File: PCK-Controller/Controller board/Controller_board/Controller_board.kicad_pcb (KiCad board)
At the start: 2 copper layers, 2 parts, among them SW1 SW_Push, U1 EC10E1260507

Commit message: Dimensions draft
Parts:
- added BT1: Battery_Cell, Battery:BatteryHolder_Keystone_1042_1x18650, F.Cu at (220.5, 100.0)
- added D1: LED, LED_SMD:LED_0603_1608Metric, B.Cu at (152.9, 124.6)
- added D10: LED, LED_SMD:LED_0603_1608Metric, B.Cu at (172.2, 135.6)
- added D11: LED, LED_SMD:LED_0603_1608Metric, B.Cu at (146.1, 137.5)
- added D12: LED, LED_SMD:LED_0603_1608Metric, B.Cu at (120.0, 135.6)
- added D13: LED, LED_SMD:LED_0603_1608Metric, B.Cu at (93.5, 135.6)
- added D14: LED, LED_SMD:LED_0603_1608Metric, B.Cu at (83.5, 114.8)
- added D15: LED, LED_SMD:LED_0603_1608Metric, B.Cu at (83.5, 66.2)
- added D2: LED, LED_SMD:LED_0603_1608Metric, B.Cu at (148.4, 124.6)
- added D3: LED, LED_SMD:LED_0603_1608Metric, B.Cu at (143.9, 124.6)
- added D4: LED, LED_SMD:LED_0603_1608Metric, B.Cu at (139.4, 124.6)
- added D5: LED, LED_SMD:LED_0603_1608Metric, B.Cu at (208.8, 66.2)
- added D6: LED, LED_SMD:LED_0603_1608Metric, B.Cu at (208.8, 82.8)
- added D7: LED, LED_SMD:LED_0603_1608Metric, B.Cu at (208.8, 98.2)
- added D8: LED, LED_SMD:LED_0603_1608Metric, B.Cu at (208.8, 114.8)
- added D9: LED, LED_SMD:LED_0603_1608Metric, B.Cu at (198.8, 135.6)
- added H1: MountingHole_Pad, MountingHole:MountingHole_3.2mm_M3_DIN965_Pad, F.Cu at (71.8, 55.6)
- added H10: MountingHole_Pad, MountingHole:MountingHole_3.2mm_M3_DIN965_Pad, F.Cu at (185.5, 124.5)
- added H11: MountingHole_Pad, MountingHole:MountingHole_3.2mm_M3_DIN965_Pad, F.Cu at (228.2, 144.4)
- added H2: MountingHole_Pad, MountingHole:MountingHole_3.2mm_M3_DIN965_Pad, F.Cu at (110.1, 56.5)
- added H3: MountingHole_Pad, MountingHole:MountingHole_3.2mm_M3_DIN965_Pad, F.Cu at (147.6, 56.5)
- added H4: MountingHole_Pad, MountingHole:MountingHole_3.2mm_M3_DIN965_Pad, F.Cu at (185.1, 56.5)
- added H5: MountingHole_Pad, MountingHole:MountingHole_3.2mm_M3_DIN965_Pad, F.Cu at (228.2, 55.6)
- added H6: MountingHole_Pad, MountingHole:MountingHole_3.2mm_M3_DIN965_Pad, F.Cu at (71.8, 144.4)
- added H7: MountingHole_Pad, MountingHole:MountingHole_3.2mm_M3_DIN965_Pad, F.Cu at (106.8, 124.5)
- added H8: MountingHole_Pad, MountingHole:MountingHole_3.2mm_M3_DIN965_Pad, F.Cu at (132.8, 145.4)
- added H9: MountingHole_Pad, MountingHole:MountingHole_3.2mm_M3_DIN965_Pad, F.Cu at (159.5, 145.4)
- added J1: Conn_01x40, FPC_P0.50mm_Horizontal_40P:FPC_P0.50mm_Horizontal_40P, F.Cu at (178.0, 90.5)
- added J2: Conn_01x06, FPC_P0.50mm_Horizontal_40P:Hirose_FH12-6S-0.5SH_1x06-1MP_P0.50mm_Horizontal, F.Cu at (184.5, 81.0)
- added J3: RJE05-166-1310, SamacSys_Parts.pretty:RJE051661310, F.Cu at (78.9, 135.3)
- added J4: USB_C_Receptacle_USB2.0_14P, Connector_USB:USB_C_Receptacle_HCTL_HC-TYPE-C-16P-01A, F.Cu at (82.1, 52.8)
- added SW10: SW_Push, Button_Switch_SMD:SW_SPST_PTS645Sx43SMTR92, B.Cu at (91.2, 114.8)
- added SW11: SW_Push, Button_Switch_SMD:SW_SPST_PTS645Sx43SMTR92, B.Cu at (91.2, 66.2)
- added SW2: SW_Push, Button_Switch_SMD:SW_SPST_PTS645Sx43SMTR92, B.Cu at (201.1, 66.2)
- added SW3: SW_Push, Button_Switch_SMD:SW_SPST_PTS645Sx43SMTR92, B.Cu at (201.1, 82.8)
- added SW4: SW_Push, Button_Switch_SMD:SW_SPST_PTS645Sx43SMTR92, B.Cu at (201.1, 98.2)
- added SW5: SW_Push, Button_Switch_SMD:SW_SPST_PTS645Sx43SMTR92, B.Cu at (201.1, 114.8)
- added SW6: SW_Push, Button_Switch_SMD:SW_SPST_PTS645Sx43SMTR92, B.Cu at (198.8, 127.1)
- added SW7: SW_Push, Button_Switch_SMD:SW_SPST_PTS645Sx43SMTR92, B.Cu at (172.2, 127.1)
- added SW8: SW_Push, Button_Switch_SMD:SW_SPST_PTS645Sx43SMTR92, B.Cu at (120.0, 127.1)
- added SW9: SW_Push, Button_Switch_SMD:SW_SPST_PTS645Sx43SMTR92, B.Cu at (93.5, 127.1)
- SW1: footprint SamacSys_Parts.pretty:EVQP0E07K -> Button_Switch_SMD:SW_SPST_PTS645Sx43SMTR92; moved to B.Cu
- U1: value EC10E1260507 -> STM32U575VITx; footprint SamacSys_Parts.pretty:EC10E1260507 -> Package_QFP:LQFP-100_14x14mm_P0.5mm
- moved SW1 60.8 mm to (146.1, 129.5), turned to 0 degrees
- moved U1 31.8 mm to (125.3, 91.1)
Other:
- board outline added: 162.5 x 99.8 mm

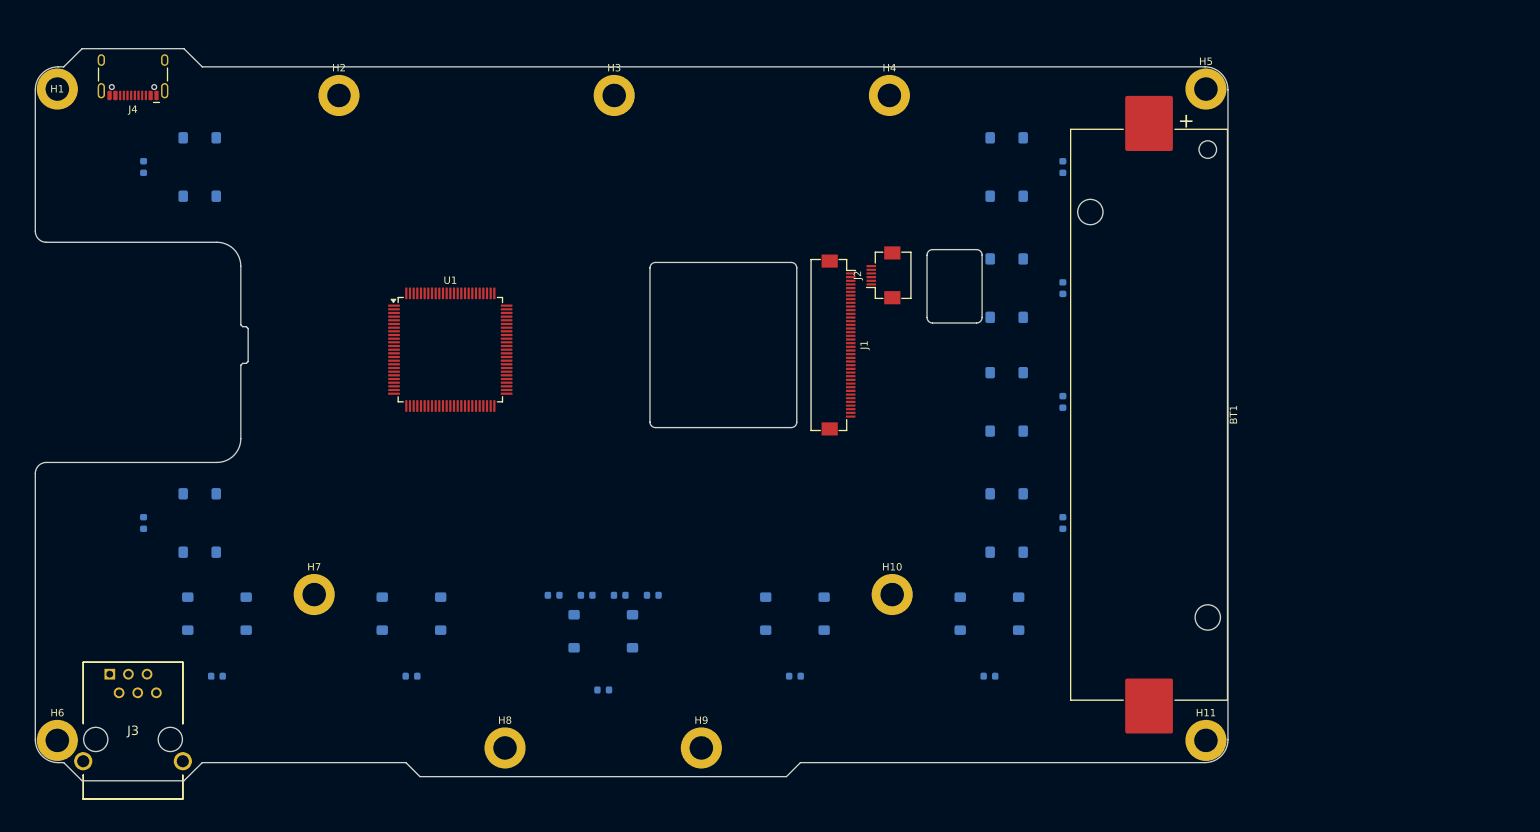
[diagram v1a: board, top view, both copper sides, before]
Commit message: Power schematic
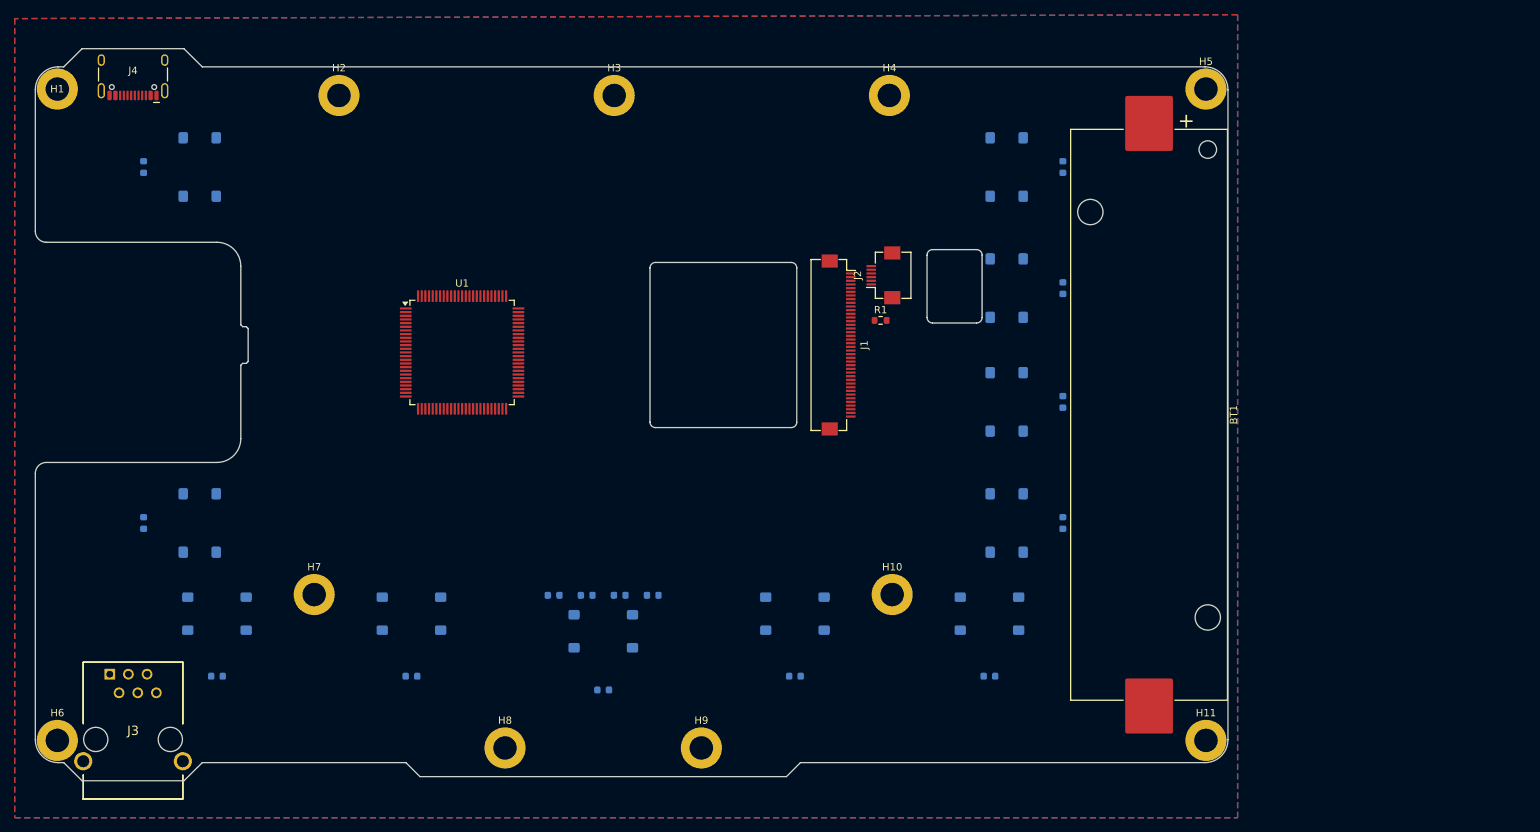
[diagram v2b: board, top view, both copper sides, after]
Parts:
- added R1: 100k, Resistor_SMD:R_0603_1608Metric, F.Cu at (183.9, 87.1)
- moved U1 1.64 mm to (126.9, 91.5)
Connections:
- J1 pad 10: unconnected-(J1-Pin_10-Pad10) -> /MCU/LCD_RS
- J1 pad 11: unconnected-(J1-Pin_11-Pad11) -> /MCU/LCD_WR
- J1 pad 12: unconnected-(J1-Pin_12-Pad12) -> /MCU/LCD_RD
- J1 pad 13: unconnected-(J1-Pin_13-Pad13) -> /MCU/LCD_SDA
- J1 pad 14: unconnected-(J1-Pin_14-Pad14) -> /MCU/LCD_SDO
- J1 pad 15: unconnected-(J1-Pin_15-Pad15) -> /MCU/LCD_RST
- J1 pad 16: unconnected-(J1-Pin_16-Pad16) -> GND
- J1 pad 17: unconnected-(J1-Pin_17-Pad17) -> /MCU/LCD_DB0
- J1 pad 18: unconnected-(J1-Pin_18-Pad18) -> /MCU/LCD_DB1
- J1 pad 19: unconnected-(J1-Pin_19-Pad19) -> /MCU/LCD_DB2
- J1 pad 20: unconnected-(J1-Pin_20-Pad20) -> /MCU/LCD_DB3
- J1 pad 21: unconnected-(J1-Pin_21-Pad21) -> /MCU/LCD_DB4
- J1 pad 22: unconnected-(J1-Pin_22-Pad22) -> /MCU/LCD_DB5
- J1 pad 23: unconnected-(J1-Pin_23-Pad23) -> /MCU/LCD_DB6
- J1 pad 24: unconnected-(J1-Pin_24-Pad24) -> /MCU/LCD_DB7
- J1 pad 25: unconnected-(J1-Pin_25-Pad25) -> /MCU/LCD_DB8
- J1 pad 26: unconnected-(J1-Pin_26-Pad26) -> /MCU/LCD_DB9
- J1 pad 27: unconnected-(J1-Pin_27-Pad27) -> /MCU/LCD_DB10
- J1 pad 28: unconnected-(J1-Pin_28-Pad28) -> /MCU/LCD_DB11
- J1 pad 29: unconnected-(J1-Pin_29-Pad29) -> /MCU/LCD_DB12
- J1 pad 30: unconnected-(J1-Pin_30-Pad30) -> /MCU/LCD_DB13
- J1 pad 31: unconnected-(J1-Pin_31-Pad31) -> /MCU/LCD_DB14
- J1 pad 32: unconnected-(J1-Pin_32-Pad32) -> /MCU/LCD_DB15
- J1 pad 33: unconnected-(J1-Pin_33-Pad33) -> /MCU/LCD_LED_A
- J1 pad 34: unconnected-(J1-Pin_34-Pad34) -> /MCU/LCD_LED_K1
- J1 pad 35: unconnected-(J1-Pin_35-Pad35) -> /MCU/LCD_LED_K2
- J1 pad 36: unconnected-(J1-Pin_36-Pad36) -> /MCU/LCD_LED_K3
- J1 pad 37: unconnected-(J1-Pin_37-Pad37) -> GND
- J1 pad 38: unconnected-(J1-Pin_38-Pad38) -> /MCU/LCD_IM0
- J1 pad 39: unconnected-(J1-Pin_39-Pad39) -> /MCU/LCD_IM1
- J1 pad 40: unconnected-(J1-Pin_40-Pad40) -> /MCU/LCD_IM2
- J1 pad 5: unconnected-(J1-Pin_5-Pad5) -> GND
- J1 pad 6: unconnected-(J1-Pin_6-Pad6) -> +3V3
- J1 pad 7: unconnected-(J1-Pin_7-Pad7) -> +3V3
- J1 pad 8: unconnected-(J1-Pin_8-Pad8) -> /MCU/LCD_TE
- J1 pad 9: unconnected-(J1-Pin_9-Pad9) -> /MCU/LCD_CS
- J2 pad 1: unconnected-(J2-Pin_1-Pad1) -> +3V3
- J2 pad 2: unconnected-(J2-Pin_2-Pad2) -> /MCU/TCH_SDA
- J2 pad 3: unconnected-(J2-Pin_3-Pad3) -> /MCU/TCH_SCL
- J2 pad 4: unconnected-(J2-Pin_4-Pad4) -> /MCU/TCH_INT
- J2 pad 5: unconnected-(J2-Pin_5-Pad5) -> /MCU/TCH_RST
- J2 pad 6: unconnected-(J2-Pin_6-Pad6) -> GND
- U1 pad 38: unconnected-(U1-PE7-Pad38) -> /MCU/LCD_DB4
- U1 pad 39: unconnected-(U1-PE8-Pad39) -> /MCU/LCD_DB5
- U1 pad 40: unconnected-(U1-PE9-Pad40) -> /MCU/LCD_DB6
- U1 pad 41: unconnected-(U1-PE10-Pad41) -> /MCU/LCD_DB7
- U1 pad 42: unconnected-(U1-PE11-Pad42) -> /MCU/LCD_DB8
- U1 pad 43: unconnected-(U1-PE12-Pad43) -> /MCU/LCD_DB9
- U1 pad 44: unconnected-(U1-PE13-Pad44) -> /MCU/LCD_DB10
- U1 pad 45: unconnected-(U1-PE14-Pad45) -> /MCU/LCD_DB11
- U1 pad 46: unconnected-(U1-PE15-Pad46) -> /MCU/LCD_DB12
- U1 pad 55: unconnected-(U1-PD8-Pad55) -> /MCU/LCD_DB13
- U1 pad 56: unconnected-(U1-PD9-Pad56) -> /MCU/LCD_DB14
- U1 pad 57: unconnected-(U1-PD10-Pad57) -> /MCU/LCD_DB15
- U1 pad 61: unconnected-(U1-PD14-Pad61) -> /MCU/LCD_DB0
- U1 pad 62: unconnected-(U1-PD15-Pad62) -> /MCU/LCD_DB1
- U1 pad 81: unconnected-(U1-PD0-Pad81) -> /MCU/LCD_DB2
- U1 pad 82: unconnected-(U1-PD1-Pad82) -> /MCU/LCD_DB3
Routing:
- added copper zone on B.Cu, net GND
- added copper zone on F.Cu, net GND

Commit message: .
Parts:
- added C1: 1uF, Capacitor_SMD:C_0603_1608Metric, F.Cu at (243.5, 76.0)
- added C10: 10u, Capacitor_SMD:C_0603_1608Metric, F.Cu at (247.5, 81.0)
- added C11: 1u, Capacitor_SMD:C_0603_1608Metric, F.Cu at (247.5, 83.6)
- added C12: 1u, Capacitor_SMD:C_0603_1608Metric, F.Cu at (247.5, 86.1)
- added C13: 1u, Capacitor_SMD:C_0603_1608Metric, F.Cu at (266.0, 81.6)
- added C14: 100n, Capacitor_SMD:C_0603_1608Metric, F.Cu at (266.0, 84.1)
- added C15: 100n, Capacitor_SMD:C_0603_1608Metric, F.Cu at (266.0, 86.6)
- added C16: 100n, Capacitor_SMD:C_0603_1608Metric, F.Cu at (266.0, 89.2)
- added C17: 100n, Capacitor_SMD:C_0603_1608Metric, F.Cu at (266.0, 91.7)
- added C18: 100n, Capacitor_SMD:C_0603_1608Metric, F.Cu at (266.0, 94.2)
- added C19: 100n, Capacitor_SMD:C_0603_1608Metric, F.Cu at (270.0, 81.6)
- added C2: 10uF, Capacitor_SMD:C_0603_1608Metric, F.Cu at (243.5, 78.5)
- added C20: 100n, Capacitor_SMD:C_0603_1608Metric, F.Cu at (270.0, 84.1)
- added C21: 100n, Capacitor_SMD:C_0603_1608Metric, F.Cu at (270.0, 86.6)
- added C22: 10u, Capacitor_SMD:C_0603_1608Metric, F.Cu at (270.0, 89.2)
- added C3: 1uF, Capacitor_SMD:C_0603_1608Metric, F.Cu at (243.5, 81.0)
- added C4: 100n, Capacitor_SMD:C_0603_1608Metric, F.Cu at (243.5, 83.6)
- added C5: 100n, Capacitor_SMD:C_0603_1608Metric, F.Cu at (243.5, 86.1)
- added C6: 10u, Capacitor_SMD:C_0603_1608Metric, F.Cu at (243.5, 88.6)
- added C7: 10u, Capacitor_SMD:C_0603_1608Metric, F.Cu at (243.5, 91.1)
- added C8: 100n, Capacitor_SMD:C_0603_1608Metric, F.Cu at (247.5, 76.0)
- added C9: 10u, Capacitor_SMD:C_0603_1608Metric, F.Cu at (247.5, 78.5)
- added IC1: BQ25185DLHR, SamacSys_Parts.pretty:SON40P220X200X80-11N, F.Cu at (259.8, 90.7)
- added IC2: TPS63030DSKT, SamacSys_Parts.pretty:SON50P250X250X80-11N-D, F.Cu at (260.0, 86.5)
- added IC3: TPS2113ADRBR, SamacSys_Parts.pretty:SON65P300X300X100-9N-D, F.Cu at (260.2, 81.8)
- added IC4: TPS78233DDCR, SamacSys_Parts.pretty:SOT95P280X110-5N, F.Cu at (260.2, 77.1)
- added L1: 1.5u, Inductor_SMD:L_1008_2520Metric, F.Cu at (261.5, 105.1)
- added R10: 1k, Resistor_SMD:R_0603_1608Metric, F.Cu at (247.5, 98.3)
- added R11: 1k, Resistor_SMD:R_0603_1608Metric, F.Cu at (247.5, 100.8)
- added R12: 1k, Resistor_SMD:R_0603_1608Metric, F.Cu at (247.5, 103.3)
- added R13: 1k, Resistor_SMD:R_0603_1608Metric, F.Cu at (247.5, 105.8)
- added R14: 1k, Resistor_SMD:R_0603_1608Metric, F.Cu at (247.5, 108.3)
- added R15: 1k, Resistor_SMD:R_0603_1608Metric, F.Cu at (247.5, 110.8)
- added R16: 100k, Resistor_SMD:R_0603_1608Metric, F.Cu at (251.5, 95.8)
- added R17: 10k, Resistor_SMD:R_0603_1608Metric, F.Cu at (247.5, 88.6)
- added R18: 10k, Resistor_SMD:R_0603_1608Metric, F.Cu at (247.5, 91.1)
- added R19: 5k1, Resistor_SMD:R_0603_1608Metric, F.Cu at (251.5, 76.0)
- added R2: 1k, Resistor_SMD:R_0603_1608Metric, F.Cu at (243.5, 95.8)
- added R20: 5k1, Resistor_SMD:R_0603_1608Metric, F.Cu at (251.5, 78.5)
- added R21: 300R, Resistor_SMD:R_0603_1608Metric, F.Cu at (251.5, 81.0)
- added R22: 13k, Resistor_SMD:R_0603_1608Metric, F.Cu at (251.5, 83.6)
- added R23: 100k, Resistor_SMD:R_0603_1608Metric, F.Cu at (251.5, 86.1)
- added R24: 22R, Resistor_SMD:R_0603_1608Metric, F.Cu at (80.5, 61.1)
- added R25: 1k, Resistor_SMD:R_0603_1608Metric, F.Cu at (251.5, 91.1)
- added R26: 10k, Resistor_SMD:R_0603_1608Metric, F.Cu at (255.6, 76.0)
- added R27: 49k9, Resistor_SMD:R_0603_1608Metric, F.Cu at (255.6, 78.5)
- added R28: 330k, Resistor_SMD:R_0603_1608Metric, F.Cu at (255.6, 81.0)
- added R29: 100k, Resistor_SMD:R_0603_1608Metric, F.Cu at (255.6, 83.6)
- added R3: 1k, Resistor_SMD:R_0603_1608Metric, F.Cu at (243.5, 98.3)
- added R30: 47k, Resistor_SMD:R_0603_1608Metric, F.Cu at (255.6, 86.1)
- added R31: 100k, Resistor_SMD:R_0603_1608Metric, F.Cu at (255.6, 88.6)
- added R32: 100k, Resistor_SMD:R_0603_1608Metric, F.Cu at (251.5, 98.3)
- added R33: 100k, Resistor_SMD:R_0603_1608Metric, F.Cu at (251.5, 100.8)
- added R34: 100k, Resistor_SMD:R_0603_1608Metric, F.Cu at (251.5, 103.3)
- added R35: 100k, Resistor_SMD:R_0603_1608Metric, F.Cu at (251.5, 105.8)
- added R36: 100k, Resistor_SMD:R_0603_1608Metric, F.Cu at (251.5, 108.3)
- added R37: 100k, Resistor_SMD:R_0603_1608Metric, F.Cu at (251.5, 110.8)
- added R38: 100k, Resistor_SMD:R_0603_1608Metric, F.Cu at (255.6, 95.8)
- added R39: 100k, Resistor_SMD:R_0603_1608Metric, F.Cu at (255.6, 98.3)
- added R4: 1k, Resistor_SMD:R_0603_1608Metric, F.Cu at (243.5, 100.8)
- added R40: 100k, Resistor_SMD:R_0603_1608Metric, F.Cu at (255.6, 100.8)
- added R41: 100k, Resistor_SMD:R_0603_1608Metric, F.Cu at (255.6, 103.3)
- added R42: 100k, Resistor_SMD:R_0603_1608Metric, F.Cu at (255.6, 105.8)
- added R43: 22R, Resistor_SMD:R_0603_1608Metric, F.Cu at (83.4, 61.1)
- added R44: 10k, Resistor_SMD:R_0603_1608Metric, F.Cu at (260.6, 97.1)
- added R45: 10k, Resistor_SMD:R_0603_1608Metric, F.Cu at (260.6, 99.6)
- added R46: 10k, Resistor_SMD:R_0603_1608Metric, F.Cu at (239.2, 71.4)
- added R5: 1k, Resistor_SMD:R_0603_1608Metric, F.Cu at (243.5, 103.3)
- added R6: 1k, Resistor_SMD:R_0603_1608Metric, F.Cu at (243.5, 105.8)
- added R7: 1k, Resistor_SMD:R_0603_1608Metric, F.Cu at (243.5, 108.3)
- added R8: 1k, Resistor_SMD:R_0603_1608Metric, F.Cu at (243.5, 110.8)
- added R9: 1k, Resistor_SMD:R_0603_1608Metric, F.Cu at (247.5, 95.8)
- added TH1: 10k, Connector_JST:JST_PH_B2B-PH-K_1x02_P2.00mm_Vertical, F.Cu at (206.4, 125.8)
- BT1: value Battery_Cell -> 18650
- R1: value 100k -> 1k
- moved U1 3.25 mm to (130.0, 92.5)
- renumbered D11 to D1, D14 to D10, D15 to D11, D1 to D12, D2 to D13, D3 to D14, D4 to D15, D5 to D2, D6 to D3, D7 to D4, D8 to D5, D9 to D6, D10 to D7, D12 to D8, D13 to D9
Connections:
- net Net-(J4-VBUS-PadA4) renamed VBUS
- BT1 pad 1: unconnected-(BT1-+-Pad1) -> Net-(BT1-+)
- BT1 pad 2: unconnected-(BT1---Pad2) -> GND
- D1 pad 1: unconnected-(D11-K-Pad1) -> GND
- D1 pad 2: unconnected-(D11-A-Pad2) -> Net-(D1-A)
- D10 pad 1: unconnected-(D14-K-Pad1) -> GND
- D10 pad 2: unconnected-(D14-A-Pad2) -> Net-(D10-A)
- D11 pad 1: unconnected-(D15-K-Pad1) -> GND
- D11 pad 2: unconnected-(D15-A-Pad2) -> Net-(D11-A)
- D12 pad 1: unconnected-(D1-K-Pad1) -> GND
- D12 pad 2: unconnected-(D1-A-Pad2) -> Net-(D12-A)
- D13 pad 1: unconnected-(D2-K-Pad1) -> GND
- D13 pad 2: unconnected-(D2-A-Pad2) -> Net-(D13-A)
- D14 pad 1: unconnected-(D3-K-Pad1) -> GND
- D14 pad 2: unconnected-(D3-A-Pad2) -> Net-(D14-A)
- D15 pad 1: unconnected-(D4-K-Pad1) -> GND
- D15 pad 2: unconnected-(D4-A-Pad2) -> Net-(D15-A)
- D2 pad 1: unconnected-(D5-K-Pad1) -> GND
- D2 pad 2: unconnected-(D5-A-Pad2) -> Net-(D2-A)
- D3 pad 1: unconnected-(D6-K-Pad1) -> GND
- D3 pad 2: unconnected-(D6-A-Pad2) -> Net-(D3-A)
- D4 pad 1: unconnected-(D7-K-Pad1) -> GND
- D4 pad 2: unconnected-(D7-A-Pad2) -> Net-(D4-A)
- D5 pad 1: unconnected-(D8-K-Pad1) -> GND
- D5 pad 2: unconnected-(D8-A-Pad2) -> Net-(D5-A)
- D6 pad 1: unconnected-(D9-K-Pad1) -> GND
- D6 pad 2: unconnected-(D9-A-Pad2) -> Net-(D6-A)
- D7 pad 1: unconnected-(D10-K-Pad1) -> GND
- D7 pad 2: unconnected-(D10-A-Pad2) -> Net-(D7-A)
- D8 pad 1: unconnected-(D12-K-Pad1) -> GND
- D8 pad 2: unconnected-(D12-A-Pad2) -> Net-(D8-A)
- D9 pad 1: unconnected-(D13-K-Pad1) -> GND
- D9 pad 2: unconnected-(D13-A-Pad2) -> Net-(D9-A)
- J1 pad 38: /MCU/LCD_IM0 -> GND
- J1 pad 39: /MCU/LCD_IM1 -> +3V3
- J1 pad 40: /MCU/LCD_IM2 -> GND
- J3 pad 1: unconnected-(J3-Pad1) -> GND
- J3 pad 2: unconnected-(J3-Pad2) -> /MCU/STM_RX
- J3 pad 3: unconnected-(J3-Pad3) -> /MCU/STM_TX
- J3 pad 4: unconnected-(J3-Pad4) -> GND
- J3 pad 5: unconnected-(J3-Pad5) -> +5V
- J3 pad 6: unconnected-(J3-Pad6) -> +5V
- J3 pad MH1: unconnected-(J3-PadMH1) -> GND
- J3 pad MH2: unconnected-(J3-PadMH2) -> GND
- J4 pad A1: Net-(J4-GND-PadA1) -> GND
- J4 pad A12: Net-(J4-GND-PadA1) -> GND
- J4 pad A5: unconnected-(J4-CC1-PadA5) -> Net-(J4-CC1)
- J4 pad A6: unconnected-(J4-D+-PadA6) -> /Power/DP
- J4 pad A7: unconnected-(J4-D--PadA7) -> /Power/DN
- J4 pad B1: Net-(J4-GND-PadA1) -> GND
- J4 pad B12: Net-(J4-GND-PadA1) -> GND
- J4 pad B5: unconnected-(J4-CC2-PadB5) -> Net-(J4-CC2)
- J4 pad B6: unconnected-(J4-D+-PadB6) -> /Power/DP
- J4 pad B7: unconnected-(J4-D--PadB7) -> /Power/DN
- J4 pad S1: unconnected-(J4-SHIELD-PadS1) -> GND
- R1 pad 1: /MCU/LCD_SDA -> Net-(D1-A)
- R1 pad 2: GND -> /MCU/LED1
- SW1 pad 1: unconnected-(SW1-Pad1) -> +3V3
- SW1 pad 2: unconnected-(SW1-Pad2) -> /MCU/BTN1
- SW10 pad 1: unconnected-(SW10-Pad1) -> +3V3
- SW10 pad 2: unconnected-(SW10-Pad2) -> /MCU/BTN10
- SW11 pad 1: unconnected-(SW11-Pad1) -> +3V3
- SW11 pad 2: unconnected-(SW11-Pad2) -> /MCU/BTN11
- SW2 pad 1: unconnected-(SW2-Pad1) -> +3V3
- SW2 pad 2: unconnected-(SW2-Pad2) -> /MCU/BTN2
- SW3 pad 1: unconnected-(SW3-Pad1) -> +3V3
- SW3 pad 2: unconnected-(SW3-Pad2) -> /MCU/BTN3
- SW4 pad 1: unconnected-(SW4-Pad1) -> +3V3
- SW4 pad 2: unconnected-(SW4-Pad2) -> /MCU/BTN4
- SW5 pad 1: unconnected-(SW5-Pad1) -> +3V3
- SW5 pad 2: unconnected-(SW5-Pad2) -> /MCU/BTN5
- SW6 pad 1: unconnected-(SW6-Pad1) -> +3V3
- SW6 pad 2: unconnected-(SW6-Pad2) -> /MCU/BTN6
- SW7 pad 1: unconnected-(SW7-Pad1) -> +3V3
- SW7 pad 2: unconnected-(SW7-Pad2) -> /MCU/BTN7
- SW8 pad 1: unconnected-(SW8-Pad1) -> +3V3
- SW8 pad 2: unconnected-(SW8-Pad2) -> /MCU/BTN8
- SW9 pad 1: unconnected-(SW9-Pad1) -> +3V3
- SW9 pad 2: unconnected-(SW9-Pad2) -> /MCU/BTN9
- U1 pad 10: Net-(U1-VSS-Pad10) -> GND
- U1 pad 100: unconnected-(U1-VDD-Pad100) -> +3V3
- U1 pad 11: unconnected-(U1-VDD-Pad11) -> +3V3
- U1 pad 19: unconnected-(U1-VSSA-Pad19) -> GND
- U1 pad 22: unconnected-(U1-VDDA-Pad22) -> +3V3
- U1 pad 23: unconnected-(U1-PA0-Pad23) -> /MCU/STM_TX
- U1 pad 24: unconnected-(U1-PA1-Pad24) -> /MCU/STM_RX
- U1 pad 27: Net-(U1-VSS-Pad10) -> GND
- U1 pad 28: unconnected-(U1-VDD-Pad28) -> +3V3
- U1 pad 48: unconnected-(U1-VCAP-Pad48) -> Net-(U1-VCAP)
- U1 pad 49: Net-(U1-VSS-Pad10) -> GND
- U1 pad 50: unconnected-(U1-VDD-Pad50) -> +3V3
- U1 pad 58: unconnected-(U1-PD11-Pad58) -> /MCU/LCD_RS
- U1 pad 6: unconnected-(U1-VBAT-Pad6) -> +3V3
- U1 pad 70: unconnected-(U1-PA11-Pad70) -> Net-(U1-PA11)
- U1 pad 71: unconnected-(U1-PA12-Pad71) -> Net-(U1-PA12)
- U1 pad 73: unconnected-(U1-VDDUSB-Pad73) -> +3V3
- U1 pad 74: Net-(U1-VSS-Pad10) -> GND
- U1 pad 75: unconnected-(U1-VDD-Pad75) -> +3V3
- U1 pad 84: unconnected-(U1-PD3-Pad84) -> /MCU/LCD_RST
- U1 pad 85: unconnected-(U1-PD4-Pad85) -> /MCU/LCD_RD
- U1 pad 86: unconnected-(U1-PD5-Pad86) -> /MCU/LCD_WR
- U1 pad 88: unconnected-(U1-PD7-Pad88) -> /MCU/LCD_CS
- U1 pad 89: unconnected-(U1-PB3-Pad89) -> /MCU/TCH_SDA
- U1 pad 90: unconnected-(U1-PB4-Pad90) -> /MCU/TCH_RST
- U1 pad 91: unconnected-(U1-PB5-Pad91) -> /MCU/TCH_INT
- U1 pad 92: unconnected-(U1-PB6-Pad92) -> /MCU/TCH_SCL
- U1 pad 99: Net-(U1-VSS-Pad10) -> GND
